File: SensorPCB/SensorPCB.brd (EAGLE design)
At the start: 35.2 x 66 mm, 33 parts, among them T1 33u

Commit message: prepare layout
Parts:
- removed R4, R5: 100k, rcl:R0805
- moved R2 116.4 mm to (31.8, 33.0), flipped to the bottom
- moved R6 110.5 mm to (27.3, 33.0), flipped to the bottom, turned to 180 degrees
- moved R11 107.3 mm to (30.5, 19.7), flipped to the bottom, turned to 90 degrees
- moved C9 105.0 mm to (33.7, 24.1), flipped to the bottom, turned to 90 degrees
- moved C3 103.3 mm to (21.0, 2.54), flipped to the bottom
- moved C8 103.0 mm to (26.0, 2.54), flipped to the bottom, turned to 180 degrees
- moved IRF7301_SENSOR 102.6 mm to (29.8, 29.2), flipped to the bottom, turned to 270 degrees
- moved C4 100.6 mm to (33.7, 19.7), flipped to the bottom, turned to 90 degrees
- moved U$5 99.2 mm to (33.0, 64.8), flipped to the bottom, turned to 270 degrees
- moved C7 96.7 mm to (26.0, 5.71), flipped to the bottom, turned to 180 degrees
- moved C10 94.6 mm to (30.5, 24.1), flipped to the bottom, turned to 270 degrees
- moved R7 94.1 mm to (28.6, 8.89), flipped to the bottom, turned to 90 degrees
- moved R8 92.8 mm to (28.6, 13.3), flipped to the bottom, turned to 90 degrees
- moved C5 90.7 mm to (21.0, 5.71), flipped to the bottom
- moved QUARZ-HC49 88.9 mm to (32.4, 8.89), flipped to the bottom, turned to 270 degrees
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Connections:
- net N$5 renamed OSC_IN
- net N$6 renamed OSC_OUT
- removed net RX_ICP: PHD.2, R5.1
- removed net TXD_ICP: PHD.1, R4.1
- net +3V3: no longer R4.2, R5.2
- net USART2_RX_SENSOR: now also PHD.2
- net USART2_TX_SENSOR: now also PHD.1

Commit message: some updates
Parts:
- moved MCP9808 5.85 mm to (18.4, 55.2)
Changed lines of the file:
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@@
 <grid distance="0.025" unitdist="inch" unit="inch" style="lines" multiple="1" display="no" altdistance="0.025" altunitdist="inch" altunit="inch"/>
 <layers>
-<layer number="1" name="Top" color="4" fill="1" visible="yes" active="yes"/>
+<layer number="1" name="Top" color="4" fill="1" visible="no" active="yes"/>
 <layer number="16" name="Bottom" color="1" fill="1" visible="no" active="yes"/>
 <layer number="17" name="Pads" color="2" fill="1" visible="yes" active="yes"/>
@@
 <element name="STM32L051C8T6" library="STM32L051x6_LQFP48XXL" package="LQFP48" value="STM32L051X6/8" x="17.78" y="18.415" rot="MR315"/>
 <element name="T1" library="CAP_TANTAL_1206" package="1206" value="33u" x="19.05" y="3.175" rot="R180"/>
-<element name="MCP9808" library="mcp9808" package="SOP65P490X110-8N" value="MCP9808-E/MS" x="17.145" y="49.53" rot="MR0">
-<attribute name="PACKAGE" value="MSOP-8" x="17.145" y="49.53" size="1.778" layer="28" rot="MR0" display="off"/>
-<attribute name="OC_NEWARK" value="89T8871" x="17.145" y="49.53" size="1.778" layer="28" rot="MR0" display="off"/>
-<attribute name="MPN" value="MCP9808-E/MS" x="17.145" y="49.53" size="1.778" layer="28" rot="MR0" display="off"/>
-<attribute name="SUPPLIER" value="MICROCHIP" x="17.145" y="49.53" size="1.778" layer="28" rot="MR0" display="off"/>
-<attribute name="OC_FARNELL" value="2080523" x="17.145" y="49.53" size="1.778" layer="28" rot="MR0" display="off"/>
+<element name="MCP9808" library="mcp9808" package="SOP65P490X110-8N" value="MCP9808-E/MS" x="18.415" y="55.245" rot="MR0">
+<attribute name="PACKAGE" value="MSOP-8" x="18.415" y="55.245" size="1.778" layer="28" rot="MR0" display="off"/>
+<attribute name="OC_NEWARK" value="89T8871" x="18.415" y="55.245" size="1.778" layer="28" rot="MR0" display="off"/>
+<attribute name="MPN" value="MCP9808-E/MS" x="18.415" y="55.245" size="1.778" layer="28" rot="MR0" display="off"/>
+<attribute name="SUPPLIER" value="MICROCHIP" x="18.415" y="55.245" size="1.778" layer="28" rot="MR0" display="off"/>
+<attribute name="OC_FARNELL" value="2080523" x="18.415" y="55.245" size="1.778" layer="28" rot="MR0" display="off"/>
 </element>
 <element name="MINI_USB" library="con-cypressindustries" package="32005-201" value="MINI-USB-SCHIELD-32005-201" x="8.89" y="5.08" rot="R90">
@@
 <contactref element="LM3940" pad="4"/>
 <contactref element="LM3940" pad="2"/>
-<wire x1="19.177" y1="48.5648" x2="24.13" y2="62.865" width="0" layer="19" extent="16-16"/>
-<wire x1="15.113" y1="48.5648" x2="19.177" y2="48.5648" width="0" layer="19" extent="16-16"/>
-<wire x1="15.113" y1="49.1998" x2="15.113" y2="48.5648" width="0" layer="19" extent="16-16"/>
-<wire x1="15.113" y1="49.8602" x2="15.113" y2="49.1998" width="0" layer="19" extent="16-16"/>
-<wire x1="27.88" y1="39.37" x2="19.177" y2="48.5648" width="0" layer="19" extent="1-16"/>
+<wire x1="20.447" y1="54.2798" x2="24.13" y2="62.865" width="0" layer="19" extent="16-16"/>
+<wire x1="16.383" y1="54.2798" x2="20.447" y2="54.2798" width="0" layer="19" extent="16-16"/>
+<wire x1="16.383" y1="54.9148" x2="16.383" y2="54.2798" width="0" layer="19" extent="16-16"/>
+<wire x1="16.383" y1="55.5752" x2="16.383" y2="54.9148" width="0" layer="19" extent="16-16"/>
+<wire x1="27.88" y1="39.37" x2="20.447" y2="54.2798" width="0" layer="19" extent="1-16"/>
 <wire x1="27.88" y1="36.83" x2="27.88" y2="39.37" width="0" layer="19" extent="1-1"/>
 <wire x1="26.355" y1="33.02" x2="27.88" y2="36.83" width="0" layer="19" extent="1-16"/>
@@
 <wire x1="27.94" y1="42.545" x2="27.94" y2="47.53" width="0.254" layer="1"/>
 <wire x1="27.94" y1="47.53" x2="27.845" y2="47.625" width="0.254" layer="1"/>
-<wire x1="15.113" y1="50.4952" x2="20.32" y2="62.865" width="0" layer="19" extent="16-16"/>
-<wire x1="27.845" y1="47.625" x2="15.113" y2="50.4952" width="0" layer="19" extent="1-16"/>
+<wire x1="16.383" y1="56.2102" x2="20.32" y2="62.865" width="0" layer="19" extent="16-16"/>
+<wire x1="27.845" y1="47.625" x2="16.383" y2="56.2102" width="0" layer="19" extent="1-16"/>
 <wire x1="25.085" y1="2.54" x2="24.765" y2="3.175" width="0" layer="19" extent="1-16"/>
 <wire x1="21.905" y1="2.54" x2="20.45" y2="3.175" width="0" layer="19" extent="1-16"/>
@@
 <contactref element="R9" pad="1"/>
 <contactref element="MCP9808" pad="2"/>
-<wire x1="19.177" y1="49.8602" x2="12.7" y2="62.865" width="0" layer="19" extent="16-16"/>
-<wire x1="14.49195625" y1="21.349490625" x2="19.177" y2="49.8602" width="0" layer="19" extent="16-16"/>
+<wire x1="20.447" y1="55.5752" x2="12.7" y2="62.865" width="0" layer="19" extent="16-16"/>
+<wire x1="14.49195625" y1="21.349490625" x2="20.447" y2="55.5752" width="0" layer="19" extent="16-16"/>
 <wire x1="4.125" y1="20.955" x2="14.49195625" y2="21.349490625" width="0" layer="19" extent="16-16"/>
 </signal>
@@
 <contactref element="R10" pad="1"/>
 <contactref element="MCP9808" pad="1"/>
-<wire x1="19.177" y1="50.4952" x2="16.51" y2="62.865" width="0" layer="19" extent="16-16"/>
-<wire x1="14.845509375" y1="21.70304375" x2="19.177" y2="50.4952" width="0" layer="19" extent="16-16"/>
+<wire x1="20.447" y1="56.2102" x2="16.51" y2="62.865" width="0" layer="19" extent="16-16"/>
+<wire x1="14.845509375" y1="21.70304375" x2="20.447" y2="56.2102" width="0" layer="19" extent="16-16"/>
 <wire x1="4.125" y1="23.495" x2="14.845509375" y2="21.70304375" width="0" layer="19" extent="16-16"/>
 </signal>

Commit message: start routing
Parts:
- moved C6 30.1 mm to (33.0, 21.9), turned to 270 degrees
- moved R9 16.0 mm to (13.3, 33.3), turned to 180 degrees
- moved R10 12.3 mm to (13.3, 30.5), turned to 180 degrees
- moved C9 11.8 mm to (28.9, 13.3), turned to 270 degrees
- moved C4 11.5 mm to (28.9, 9.21), turned to 270 degrees
- moved R12 10.2 mm to (13.3, 28.3), turned to 180 degrees
- moved C10 4.45 mm to (30.5, 19.7)
- moved R11 4.45 mm to (30.5, 24.1), turned to 270 degrees
- moved QUARZ-HC49 2.56 mm to (32.7, 11.4)
- moved R7 2.25 mm to (26.4, 9.21)
- moved R8 2.22 mm to (26.4, 13.3), turned to 270 degrees
- moved MCP9808 1.91 mm to (18.4, 57.1), turned to 180 degrees
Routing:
- net SPI2_NSS_WLAN: track 0.00 -> 71.2 mm, vias 0 -> 1
- net SPI2_SCK_WLAN: track 0.00 -> 67.0 mm, vias 0 -> 1
- net SPI2_MOSI_WLAN: track 0.00 -> 61.2 mm, vias 0 -> 1
- net SPI2_MISO_WLAN: track 0.00 -> 57.5 mm, vias 0 -> 1
- net I2C1_SCL_SENSOR: track 0.00 -> 51.9 mm
- net I2C1_SDA_SENSOR: track 0.00 -> 51.5 mm
- net SPI1_MOSI_SENSOR: track 0.00 -> 44.0 mm
- net SPI1_MISO_SENSOR: track 0.00 -> 43.9 mm
- net OSC_IN: track 0.00 -> 40.8 mm
- net SPI1_SCK_SENSOR: track 0.00 -> 39.9 mm
- net GND_SENSOR: track 0.00 -> 39.0 mm
- net SPI1_NSS_SENSOR: track 0.00 -> 35.9 mm
- net GND_WLAN: track 0.00 -> 33.5 mm
- net ADC_WLAN: track 0.00 -> 21.1 mm
- net SWCLK: track 0.00 -> 17.7 mm
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
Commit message: routing layout beautiful but maybe not accurate
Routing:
- net USART2_RX_SENSOR: track 0.00 -> 41.7 mm
- net REST_WLAN: track 0.00 -> 41.6 mm, vias 0 -> 1
- net ADC_WLAN: track 21.1 -> 54.1 mm, vias 0 -> 1
- net USART2_TX_SENSOR: track 0.00 -> 30.5 mm
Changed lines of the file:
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@@
 <contactref element="ESP8266" pad="1"/>
 <contactref element="STM32L051C8T6" pad="29"/>
-<wire x1="15.1990625" y1="14.7734" x2="13.845" y2="47.625" width="0" layer="19" extent="1-16"/>
+<wire x1="13.845" y1="47.625" x2="13.97" y2="47.5" width="0.254" layer="1"/>
+<wire x1="13.97" y1="47.5" x2="13.97" y2="44.7675" width="0.254" layer="1"/>
+<wire x1="13.97" y1="44.7675" x2="19.05" y2="39.6875" width="0.254" layer="1"/>
+<wire x1="19.05" y1="39.6875" x2="19.05" y2="16.51" width="0.254" layer="1"/>
+<wire x1="19.05" y1="16.51" x2="15.5575" y2="13.0175" width="0.254" layer="1"/>
+<wire x1="15.5575" y1="13.0175" x2="14.2875" y2="13.0175" width="0.254" layer="1"/>
+<via x="14.2875" y="13.0175" extent="1-16" drill="0.6"/>
+<wire x1="15.1990625" y1="14.7734" x2="14.2875" y2="13.8618375" width="0.254" layer="16"/>
+<wire x1="14.2875" y1="13.8618375" x2="14.2875" y2="13.0175" width="0.254" layer="16"/>
 </signal>
 <signal name="ADC_WLAN">
@@
 <wire x1="27.6225" y1="10.16" x2="27.62" y2="10.1575" width="0.254" layer="16"/>
 <wire x1="27.62" y1="10.1575" x2="26.3525" y2="10.1575" width="0.254" layer="16"/>
-<wire x1="24.13" y1="22.225" x2="15.845" y2="47.625" width="0" layer="19" extent="1-16"/>
+<wire x1="15.845" y1="47.625" x2="15.875" y2="47.595" width="0.254" layer="1"/>
+<wire x1="15.875" y1="47.595" x2="15.875" y2="44.45" width="0.254" layer="1"/>
+<wire x1="15.875" y1="44.45" x2="20.0025" y2="40.3225" width="0.254" layer="1"/>
+<wire x1="20.0025" y1="40.3225" x2="20.0025" y2="19.05" width="0.254" layer="1"/>
+<via x="20.0025" y="19.05" extent="1-16" drill="0.6"/>
+<wire x1="22.128709375" y1="20.28883125" x2="20.889878125" y2="19.05" width="0.254" layer="16"/>
+<wire x1="20.889878125" y1="19.05" x2="20.0025" y2="19.05" width="0.254" layer="16"/>
 </signal>
 <signal name="CH_PD_WLAN">
@@
 <contactref element="STM32L051C8T6" pad="26"/>
 <contactref element="ESP8266" pad="22"/>
-<wire x1="16.259721875" y1="13.7127375" x2="19.05" y2="16.503015625" width="0.254" layer="16"/>
 <wire x1="19.05" y1="16.503015625" x2="19.05" y2="17.4625" width="0.254" layer="16"/>
 <wire x1="19.05" y1="17.4625" x2="17.78" y2="18.7325" width="0.254" layer="16"/>
@@
 <wire x1="11.1125" y1="56.515" x2="11.2225" y2="56.625" width="0.254" layer="1"/>
 <wire x1="11.2225" y1="56.625" x2="29.845" y2="56.625" width="0.254" layer="1"/>
+<wire x1="16.259721875" y1="13.7127375" x2="19.05" y2="16.503015625" width="0.254" layer="16"/>
 </signal>
 <signal name="SPI2_MISO_WLAN">
@@
 <contactref element="STM32L051C8T6" pad="28"/>
 <contactref element="ESP8266" pad="21"/>
-<wire x1="15.552615625" y1="14.41984375" x2="17.145" y2="16.012228125" width="0.254" layer="16"/>
 <wire x1="17.145" y1="16.012228125" x2="17.145" y2="17.78" width="0.254" layer="16"/>
 <via x="17.145" y="17.78" extent="1-16" drill="0.6"/>
@@
 <wire x1="11.7475" y1="54.61" x2="11.7625" y2="54.625" width="0.254" layer="1"/>
 <wire x1="11.7625" y1="54.625" x2="29.845" y2="54.625" width="0.254" layer="1"/>
+<wire x1="15.552615625" y1="14.41984375" x2="17.145" y2="16.012228125" width="0.254" layer="16"/>
 </signal>
 <signal name="SPI1_NSS_SENSOR">
@@
 <contactref element="STM32L051C8T6" pad="13"/>
 <contactref element="PHD" pad="2"/>
+<wire x1="2.54" y1="5.08" x2="1.905" y2="4.445" width="0.254" layer="16"/>
+<wire x1="1.905" y1="4.445" x2="1.905" y2="1.27" width="0.254" layer="16"/>
+<wire x1="1.905" y1="1.27" x2="2.2225" y2="0.9525" width="0.254" layer="16"/>
+<wire x1="2.2225" y1="0.9525" x2="15.5575" y2="0.9525" width="0.254" layer="16"/>
+<wire x1="15.5575" y1="0.9525" x2="18.415" y2="3.81" width="0.254" layer="16"/>
+<wire x1="22.835815625" y1="17.248271875" x2="24.4475" y2="15.6365875" width="0.254" layer="16"/>
+<wire x1="24.4475" y1="15.6365875" x2="24.4475" y2="7.62" width="0.254" layer="16"/>
+<wire x1="24.4475" y1="7.62" x2="24.13" y2="7.3025" width="0.254" layer="16"/>
+<wire x1="18.415" y1="3.81" x2="18.415" y2="6.985" width="0.254" layer="16"/>
+<wire x1="18.415" y1="6.985" x2="18.7325" y2="7.3025" width="0.254" layer="16"/>
+<wire x1="18.7325" y1="7.3025" x2="24.13" y2="7.3025" width="0.254" layer="16"/>
 <wire x1="22.835815625" y1="17.248271875" x2="31.115" y2="54.61" width="0" layer="19" extent="16-16"/>
-<wire x1="2.54" y1="5.08" x2="22.835815625" y2="17.248271875" width="0" layer="19" extent="16-16"/>
 </signal>
 <signal name="PA4">
@@
 <contactref element="U$5" pad="P$1"/>
 <contactref element="PHD" pad="1"/>
+<wire x1="5.08" y1="2.54" x2="15.5575" y2="2.54" width="0.254" layer="16"/>
+<wire x1="15.5575" y1="2.54" x2="17.78" y2="4.7625" width="0.254" layer="16"/>
+<wire x1="17.78" y1="4.7625" x2="17.78" y2="13.6525" width="0.254" layer="16"/>
+<wire x1="17.78" y1="13.6525" x2="21.59" y2="17.4625" width="0.254" layer="16"/>
+<wire x1="22.835815625" y1="19.581725" x2="21.59" y2="18.335909375" width="0.254" layer="16"/>
+<wire x1="21.59" y1="18.335909375" x2="21.59" y2="17.4625" width="0.254" layer="16"/>
 <wire x1="22.835815625" y1="19.581725" x2="31.115" y2="58.42" width="0" layer="19" extent="16-16"/>
-<wire x1="5.08" y1="2.54" x2="22.835815625" y2="19.581725" width="0" layer="19" extent="16-16"/>
 </signal>
 <signal name="ALERT">

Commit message: update layout
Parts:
- moved IRF7301_WLAN 3.17 mm to (30.5, 40.6)
- moved PHD 1.90 mm to (5.71, 3.81)
- moved LM3940 1.59 mm to (7.30, 21.6)
- moved C1 0.64 mm to (1.91, 13.3)
- moved MINI_USB 0.63 mm to (9.53, 5.08)
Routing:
- net PB2: track 0.00 -> 73.1 mm, vias 0 -> 2
- net PB1: track 0.00 -> 70.9 mm, vias 0 -> 2
- net SW_SENSOR: track 0.00 -> 64.0 mm, vias 0 -> 2
- net USART1_TX_WLAN: track 0.00 -> 61.1 mm, vias 0 -> 1
- net USART1_RX_WLAN: track 0.00 -> 57.7 mm, vias 0 -> 1
- net PB0: track 0.00 -> 57.5 mm, vias 0 -> 2
- net SW_WLAN: track 2.54 -> 54.3 mm, vias 0 -> 1
- net USART2_TX_SENSOR: track 30.5 -> 82.2 mm, vias 0 -> 2
- net +3V3: track 73.1 -> 37.2 mm
- net PA4: track 0.00 -> 25.5 mm
- net USART2_RX_SENSOR: track 41.7 -> 62.6 mm
- net PA5: track 0.00 -> 14.2 mm
- net GATE_SENSOR: track 0.00 -> 11.8 mm
- net SWCLK: track 17.7 -> 6.49 mm
- net PA6: track 0.00 -> 9.75 mm
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
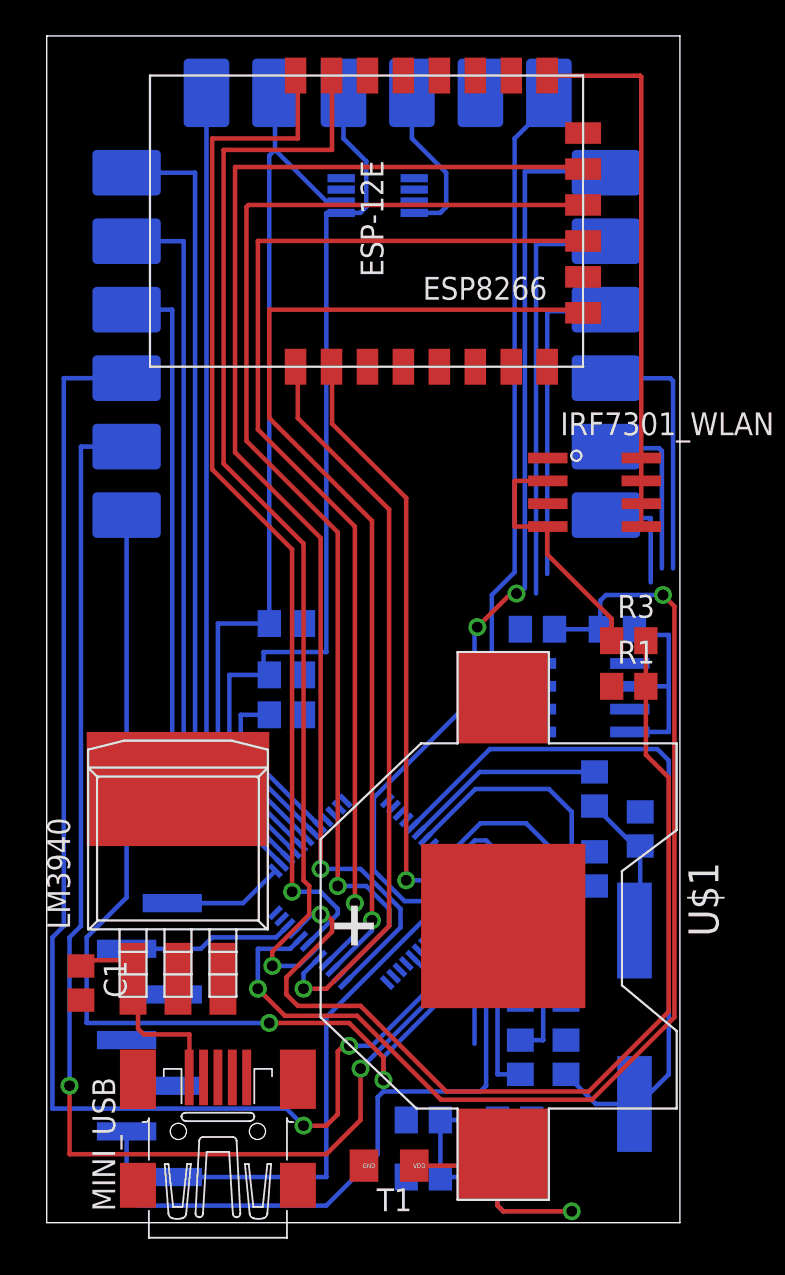
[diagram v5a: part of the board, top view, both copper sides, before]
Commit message: remote top-wires and vias from tstop layer (battery)
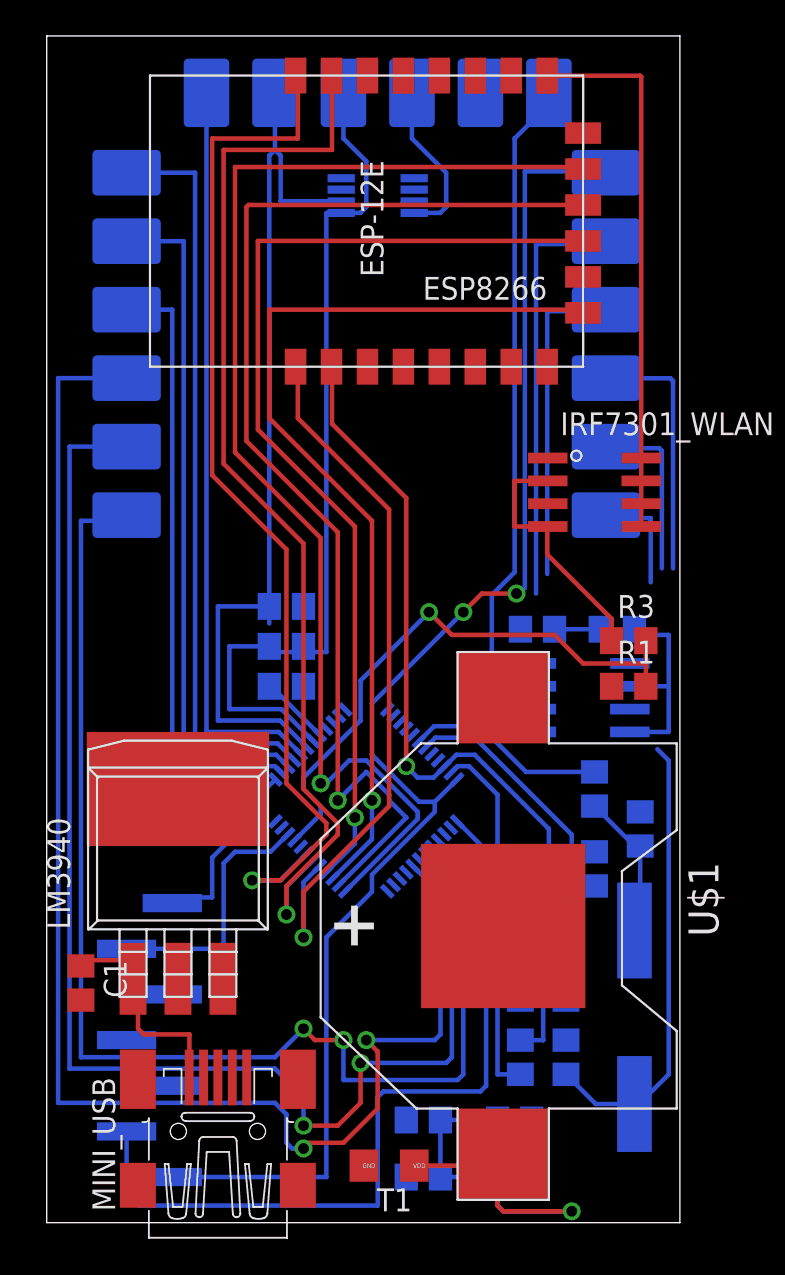
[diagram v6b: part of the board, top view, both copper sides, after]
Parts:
- moved STM32L051C8T6 5.08 mm to (17.8, 23.5)
- moved R10 1.59 mm to (13.3, 32.1)
- moved R12 1.59 mm to (13.3, 29.8)
- moved R9 0.95 mm to (13.3, 34.3)
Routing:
- net SW_SENSOR: track 64.0 -> 2.55 mm, vias 2 -> 0
- net SW_WLAN: track 54.3 -> 32.4 mm
- net OSC_IN: track 40.8 -> 25.4 mm
- net PB0: track 57.5 -> 70.2 mm
- net PB2: track 73.1 -> 83.2 mm
- net PA4: track 25.5 -> 18.0 mm
- net USART2_RX_SENSOR: track 62.6 -> 69.4 mm
- net N$8: track 9.62 -> 3.94 mm
- net SPI2_MOSI_WLAN: track 61.2 -> 56.1 mm
- net SPI2_MISO_WLAN: track 57.5 -> 52.5 mm
- net PB1: track 70.9 -> 75.9 mm
- net ADC_WLAN: track 54.1 -> 49.3 mm
- net SWDIO: track 9.53 -> 14.2 mm
- net SWCLK: track 6.49 -> 10.4 mm
- net I2C1_SDA_SENSOR: track 51.5 -> 48.3 mm
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
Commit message: layout update
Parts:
- moved IRF7301_SENSOR 0.32 mm to (30.2, 29.2)
- moved C6 0.32 mm to (33.0, 21.6)
- moved R11 0.32 mm to (30.5, 23.8)
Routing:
- net SW_SENSOR: track 2.55 -> 72.4 mm, vias 0 -> 2
- net OSC_IN: track 25.4 -> 39.9 mm
- net USART2_RX_SENSOR: track 69.4 -> 73.6 mm
- net N$4: track 8.29 -> 4.96 mm
- net N$1: track 20.2 -> 23.0 mm
- net GATE_WLAN: track 14.5 -> 15.8 mm
- net PB0: track 70.2 -> 71.6 mm
- net GND_SENSOR: track 39.0 -> 39.7 mm, vias 0 -> 2
- net PB1: track 75.9 -> 75.2 mm
- net SW_WLAN: track 32.4 -> 31.7 mm
- net GATE_SENSOR: track 11.8 -> 11.1 mm
- net REST_WLAN: track 40.2 -> 39.6 mm
- net USART2_TX_SENSOR: vias 2 -> 0
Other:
- board size 35.2 x 66 mm -> 36 x 66 mm
